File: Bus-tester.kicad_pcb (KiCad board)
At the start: 2 copper layers, 110 x 60 mm, 79 parts, among them J1 POWER, J10 In_Reg, J11 Out_Reg, J12 POWER, J2 POWER, J3 C1_out, J4 C2_out, J5 C3_out, J6 C4_out, J7 Out_sw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

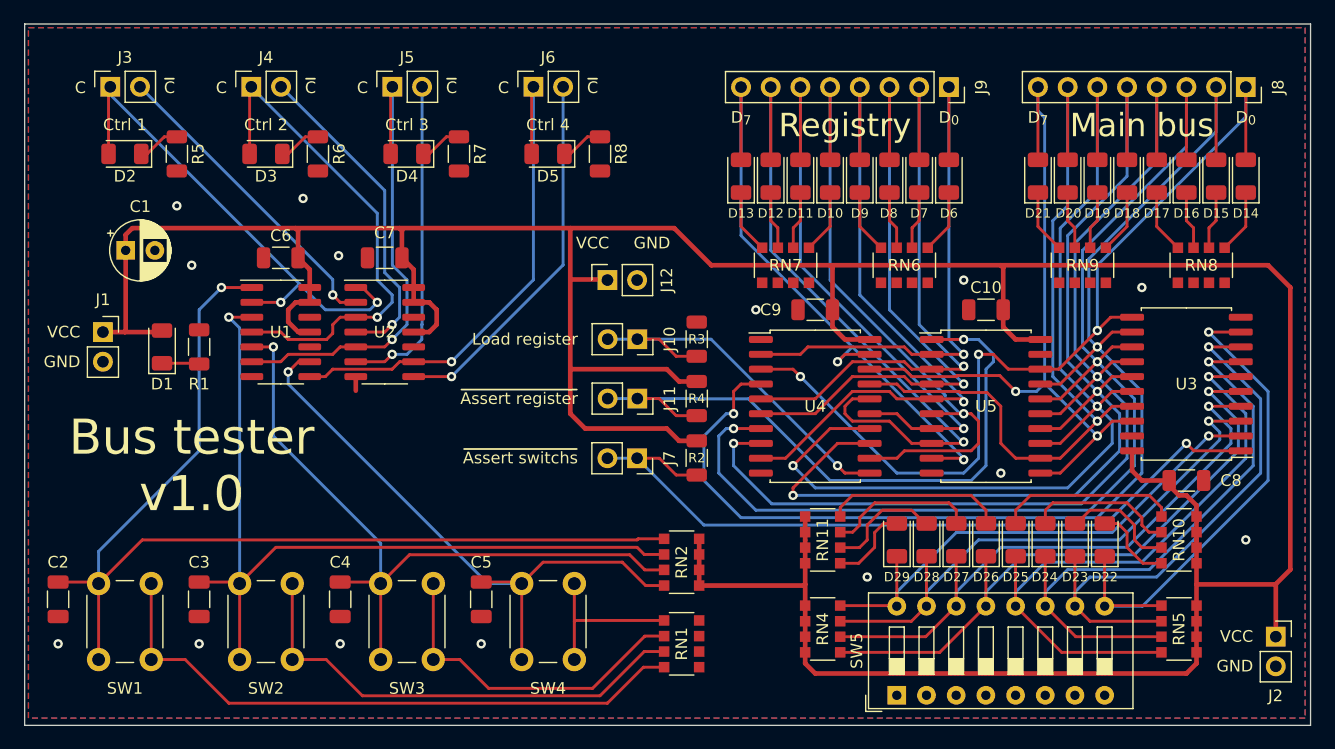
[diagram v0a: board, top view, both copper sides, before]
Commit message: optimize routing for register chip
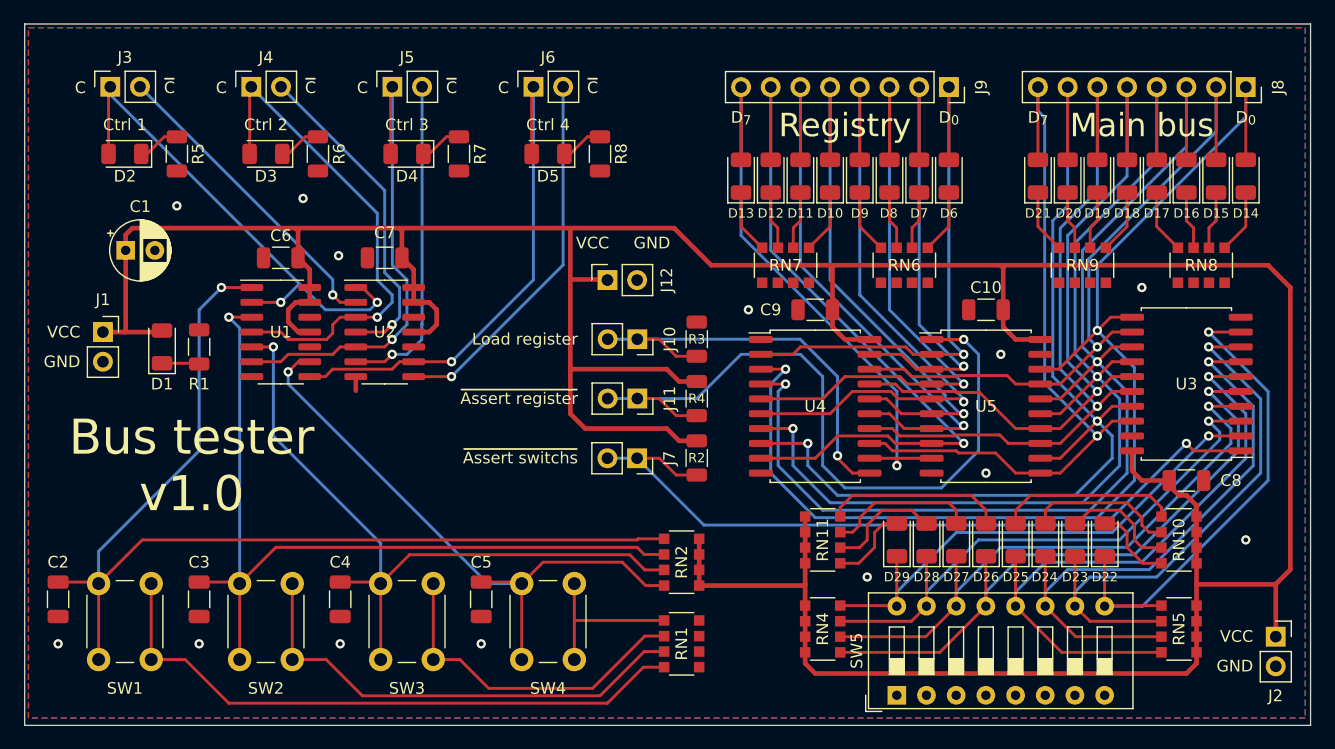
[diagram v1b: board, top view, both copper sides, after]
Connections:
- U4 pad 12: /Reg_{4} -> /Reg_{7}
- U4 pad 13: /Bus_{4} -> /Bus_{7}
- U4 pad 16: /Reg_{6} -> /Reg_{4}
- U4 pad 17: /Bus_{6} -> /Bus_{4}
- U4 pad 18: /Bus_{7} -> /Bus_{1}
- U4 pad 19: /Reg_{7} -> /Reg_{1}
- U4 pad 4: /Bus_{1} -> /Bus_{2}
- U4 pad 5: /Reg_{1} -> /Reg_{2}
- U4 pad 6: /Reg_{2} -> /Reg_{3}
- U4 pad 7: /Bus_{2} -> /Bus_{3}
- U4 pad 8: /Bus_{3} -> /Bus_{6}
- U4 pad 9: /Reg_{3} -> /Reg_{6}
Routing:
- net /Bus_{1}: track 107.3 -> 58.1 mm, vias 2 -> 1
- net /Bus_{4}: track 89.3 -> 61.3 mm, vias 2 -> 1
- net /Bus_{5}: track 87.1 -> 61.0 mm, vias 2 -> 1
- net /Bus_{0}: track 79.5 -> 101.7 mm, vias 3 -> 2
- net /Bus_{6}: track 65.7 -> 84.6 mm, vias 1 -> 2
- net /Reg_{1}: track 50.9 -> 40.5 mm
- net /Reg_{4}: track 55.1 -> 47.7 mm
- net Net-(J11-Pin_1): track 57.1 -> 62.3 mm
- net /Reg_{6}: track 57.8 -> 61.9 mm
- net Net-(J10-Pin_1): track 32.8 -> 36.9 mm
- net /Bus_{3}: track 93.3 -> 89.3 mm
- net /Reg_{7}: track 53.6 -> 50.1 mm, vias 2 -> 1
- net /Bus_{2}: track 99.3 -> 96.3 mm
- net /Reg_{3}: track 56.9 -> 55.3 mm
- net /Reg_{2}: track 53.2 -> 52.7 mm
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
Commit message: optimize routing
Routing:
- net /~{C3}: track 28.1 -> 27.3 mm
- net Net-(RN2D-R4.1): track 53.9 -> 53.3 mm
- net /C1: track 42.8 -> 42.3 mm
- net /C3: track 41.0 -> 41.6 mm
- net /C2: track 43.0 -> 43.5 mm
- net /~{C2}: track 28.2 -> 28.7 mm
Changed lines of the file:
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@@
   (segment (start 72.485 64.04) (end 74.7 64.04) (width 0.25) (layer "F.Cu") (net 3))
   (via (at 36.83 42.545) (size 0.8) (drill 0.4) (layers "F.Cu" "B.Cu") (net 3))
-  (segment (start 34.925 44.45) (end 36.83 42.545) (width 0.25) (layer "B.Cu") (net 3))
-  (segment (start 26.325 65.115) (end 34.925 56.515) (width 0.25) (layer "B.Cu") (net 3))
-  (segment (start 26.325 67.87) (end 26.325 65.115) (width 0.25) (layer "B.Cu") (net 3))
-  (segment (start 34.925 56.515) (end 34.925 44.45) (width 0.25) (layer "B.Cu") (net 3))
+  (segment (start 32.385 46.99) (end 36.83 42.545) (width 0.25) (layer "B.Cu") (net 3))
+  (segment (start 32.4925 61.7025) (end 32.385 61.595) (width 0.25) (layer "B.Cu") (net 3))
+  (segment (start 26.325 67.87) (end 32.4925 61.7025) (width 0.25) (layer "B.Cu") (net 3))
+  (segment (start 32.385 61.595) (end 32.385 46.99) (width 0.25) (layer "B.Cu") (net 3))
   (segment (start 38.39 67.87) (end 41.49 64.77) (width 0.25) (layer "F.Cu") (net 4))
   (segment (start 72.39 64.77) (end 73 65.38) (width 0.25) (layer "F.Cu") (net 4))
@@
   (segment (start 50.455 67.87) (end 50.455 74.37) (width 0.25) (layer "F.Cu") (net 5))
   (via (at 41.275 47.625) (size 0.8) (drill 0.4) (layers "F.Cu" "B.Cu") (net 5))
-  (segment (start 41.275 55.245) (end 50.455 64.425) (width 0.25) (layer "B.Cu") (net 5))
-  (segment (start 50.455 64.425) (end 50.455 67.87) (width 0.25) (layer "B.Cu") (net 5))
-  (segment (start 41.275 47.625) (end 41.275 55.245) (width 0.25) (layer "B.Cu") (net 5))
+  (segment (start 41.275 47.625) (end 41.275 58.69) (width 0.25) (layer "B.Cu") (net 5))
+  (segment (start 41.275 58.69) (end 50.455 67.87) (width 0.25) (layer "B.Cu") (net 5))
   (segment (start 42.545 49.760001) (end 43.410001 48.895) (width 0.25) (layer "F.Cu") (net 6))
   (segment (start 62.52 74.37) (end 62.52 67.87) (width 0.25) (layer "F.Cu") (net 6))
@@
   (segment (start 71.12 66.04) (end 73.12 68.04) (width 0.25) (layer "F.Cu") (net 6))
   (via (at 42.545 49.760001) (size 0.8) (drill 0.4) (layers "F.Cu" "B.Cu") (net 6))
-  (segment (start 62.52 67.87) (end 59.615 67.87) (width 0.25) (layer "B.Cu") (net 6))
-  (segment (start 42.545 50.8) (end 42.545 49.760001) (width 0.25) (layer "B.Cu") (net 6))
-  (segment (start 42.545 50.8) (end 59.615 67.87) (width 0.25) (layer "B.Cu") (net 6))
+  (segment (start 62.52 67.87) (end 60.654999 67.87) (width 0.25) (layer "B.Cu") (net 6))
+  (segment (start 60.654999 67.87) (end 42.545 49.760001) (width 0.25) (layer "B.Cu") (net 6))
   (segment (start 31.75 49.025) (end 34.8625 49.025) (width 0.25) (layer "F.Cu") (net 7))
   (segment (start 31.9425 29.6525) (end 33.02 29.6525) (width 0.25) (layer "F.Cu") (net 8))
@@
   (via (at 41.91 43.815) (size 0.8) (drill 0.4) (layers "F.Cu" "B.Cu") (net 9))
   (via (at 50.165 43.815) (size 0.8) (drill 0.4) (layers "F.Cu" "B.Cu") (net 9))
+  (segment (start 45.085 43.815) (end 43.4975 42.2275) (width 0.25) (layer "B.Cu") (net 9))
   (segment (start 41.91 43.815) (end 43.4975 42.2275) (width 0.25) (layer "B.Cu") (net 9))
-  (segment (start 50.165 43.815) (end 49.53 44.45) (width 0.25) (layer "B.Cu") (net 9))
-  (segment (start 45.72 44.45) (end 43.4975 42.2275) (width 0.25) (layer "B.Cu") (net 9))
+  (segment (start 50.165 43.815) (end 45.085 43.815) (width 0.25) (layer "B.Cu") (net 9))
   (segment (start 43.4975 42.2275) (end 27.325 26.055) (width 0.25) (layer "B.Cu") (net 9))
-  (segment (start 49.53 44.45) (end 45.72 44.45) (width 0.25) (layer "B.Cu") (net 9))
   (segment (start 44.0075 29.6525) (end 45.085 29.6525) (width 0.25) (layer "F.Cu") (net 10))
   (segment (start 42.545 31.115) (end 44.0075 29.6525) (width 0.25) (layer "F.Cu") (net 10))
@@
   (segment (start 46.99 45.085) (end 48.325 45.085) (width 0.25) (layer "F.Cu") (net 11))
   (via (at 50.165 45.085) (size 0.8) (drill 0.4) (layers "F.Cu" "B.Cu") (net 11))
-  (segment (start 51.435 43.815) (end 50.165 45.085) (width 0.25) (layer "B.Cu") (net 11))
-  (segment (start 39.39 25.42) (end 50.165 36.195) (width 0.25) (layer "B.Cu") (net 11))
-  (segment (start 50.165 36.195) (end 50.165 41.91) (width 0.25) (layer "B.Cu") (net 11))
-  (segment (start 50.165 41.91) (end 51.435 43.18) (width 0.25) (layer "B.Cu") (net 11))
-  (segment (start 51.435 43.18) (end 51.435 43.815) (width 0.25) (layer "B.Cu") (net 11))
+  (segment (start 50.165 45.085) (end 52.07 43.18) (width 0.25) (layer "B.Cu") (net 11))
+  (segment (start 52.07 43.18) (end 52.07 38.1) (width 0.25) (layer "B.Cu") (net 11))
+  (segment (start 52.07 38.1) (end 39.39 25.42) (width 0.25) (layer "B.Cu") (net 11))
   (segment (start 54.61 31.115) (end 56.0725 29.6525) (width 0.25) (layer "F.Cu") (net 12))
   (segment (start 54.105 31.115) (end 54.61 31.115) (width 0.25) (layer "F.Cu") (net 12))
@@
   (segment (start 46.99 47.625) (end 48.325 47.625) (width 0.25) (layer "F.Cu") (net 13))
   (via (at 51.435 46.99) (size 0.8) (drill 0.4) (layers "F.Cu" "B.Cu") (net 13))
-  (segment (start 51.435 46.99) (end 52.705 45.72) (width 0.25) (layer "B.Cu") (net 13))
-  (segment (start 51.455 25.375) (end 51.455 40.64) (width 0.25) (layer "B.Cu") (net 13))
-  (segment (start 52.705 45.72) (end 52.705 41.89) (width 0.25) (layer "B.Cu") (net 13))
-  (segment (start 52.705 41.89) (end 51.455 40.64) (width 0.25) (layer "B.Cu") (net 13))
+  (segment (start 52.705 29.845) (end 53.34 30.48) (width 0.25) (layer "B.Cu") (net 13))
+  (segment (start 52.705 29.825) (end 52.705 29.845) (width 0.25) (layer "B.Cu") (net 13))
+  (segment (start 51.455 25.375) (end 51.455 28.575) (width 0.25) (layer "B.Cu") (net 13))
+  (segment (start 53.34 45.085) (end 51.435 46.99) (width 0.25) (layer "B.Cu") (net 13))
+  (segment (start 51.455 28.575) (end 52.705 29.825) (width 0.25) (layer "B.Cu") (net 13))
+  (segment (start 53.34 30.48) (end 53.34 45.085) (width 0.25) (layer "B.Cu") (net 13))
   (segment (start 68.1375 29.6525) (end 69.215 29.6525) (width 0.25) (layer "F.Cu") (net 14))
   (segment (start 66.17 31.115) (end 66.675 31.115) (width 0.25) (layer "F.Cu") (net 14))
@@
   (segment (start 92.71 63.5) (end 92.71 64.77) (width 0.25) (layer "F.Cu") (net 63))
   (segment (start 46.99 43.815) (end 46.355 43.18) (width 0.25) (layer "F.Cu") (net 64))
+  (segment (start 46.355 43.18) (end 46.355 41.91) (width 0.25) (layer "F.Cu") (net 64))
   (segment (start 48.325 43.815) (end 46.99 43.815) (width 0.25) (layer "F.Cu") (net 64))
-  (via (at 46.355 43.18) (size 0.8) (drill 0.4) (layers "F.Cu" "B.Cu") (net 64))
-  (segment (start 46.355 43.18) (end 46.355 41.865) (width 0.25) (layer "B.Cu") (net 64))
+  (via (at 46.355 41.91) (size 0.8) (drill 0.4) (layers "F.Cu" "B.Cu") (net 64))
   (segment (start 46.355 41.865) (end 29.865 25.375) (width 0.25) (layer "B.Cu") (net 64))
   (segment (start 50.8 46.355) (end 51.435 45.72) (width 0.25) (layer "F.Cu") (net 65))
   (segment (start 48.325 46.355) (end 50.8 46.355) (width 0.25) (layer "F.Cu") (net 65))
   (via (at 51.435 45.72) (size 0.8) (drill 0.4) (layers "F.Cu" "B.Cu") (net 65))
-  (segment (start 50.8 41.275) (end 52.07 42.545) (width 0.25) (layer "B.Cu") (net 65))
-  (segment (start 52.07 42.545) (end 52.07 45.085) (width 0.25) (layer "B.Cu") (net 65))
-  (segment (start 50.8 34.245) (end 50.8 41.275) (width 0.25) (layer "B.Cu") (net 65))
-  (segment (start 52.07 45.085) (end 51.435 45.72) (width 0.25) (layer "B.Cu") (net 65))
-  (segment (start 41.93 25.375) (end 50.8 34.245) (width 0.25) (layer "B.Cu") (net 65))
+  (segment (start 52.705 44.45) (end 52.705 36.15) (width 0.25) (layer "B.Cu") (net 65))
+  (segment (start 51.435 45.72) (end 52.705 44.45) (width 0.25) (layer "B.Cu") (net 65))
+  (segment (start 52.705 36.15) (end 41.93 25.375) (width 0.25) (layer "B.Cu") (net 65))
   (segment (start 50.8 48.895) (end 51.435 48.26) (width 0.25) (layer "F.Cu") (net 66))
   (segment (start 48.325 48.895) (end 50.8 48.895) (width 0.25) (layer "F.Cu") (net 66))
   (via (at 51.435 48.26) (size 0.8) (drill 0.4) (layers "F.Cu" "B.Cu") (net 66))
-  (segment (start 53.975 46.99) (end 53.975 45.72) (width 0.25) (layer "B.Cu") (net 66))
-  (segment (start 53.975 45.72) (end 53.995 45.7) (width 0.25) (layer "B.Cu") (net 66))
-  (segment (start 52.705 48.26) (end 53.975 46.99) (width 0.25) (layer "B.Cu") (net 66))
   (segment (start 53.995 45.7) (end 53.995 25.375) (width 0.25) (layer "B.Cu") (net 66))
-  (segment (start 51.435 48.26) (end 52.705 48.26) (width 0.25) (layer "B.Cu") (net 66))
+  (segment (start 51.435 48.26) (end 53.995 45.7) (width 0.25) (layer "B.Cu") (net 66))
   (segment (start 53.275 50.165) (end 56.515 50.165) (width 0.25) (layer "F.Cu") (net 67))
   (via (at 56.515 50.165) (size 0.8) (drill 0.4) (layers "F.Cu" "B.Cu") (net 67))
